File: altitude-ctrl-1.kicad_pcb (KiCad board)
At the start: 2 copper layers, 90 x 90 mm, 93 parts, among them J1 Conn_01x02, J10 Conn_01x02, J11 Conn_01x04, J2 Conn_01x02, J3 Conn_01x05, J4 TC2030, J5 Conn_01x04_Pin, J6 Conn_01x02, J7 Conn_01x05, J8 Conn_01x05, J9 Conn_01x02, SW1 SW_Push, SW2 SW_SPST, SW3 SW_Push, SW4 SW_SPST, SW5 SW_Push, U1 HT753-1, U2 ULN2003A, U3 LM73100, U4 LM73100, U5 MAX6675, U6 STM32F103C8Tx, U7 SN65HVD230, Y1 8M

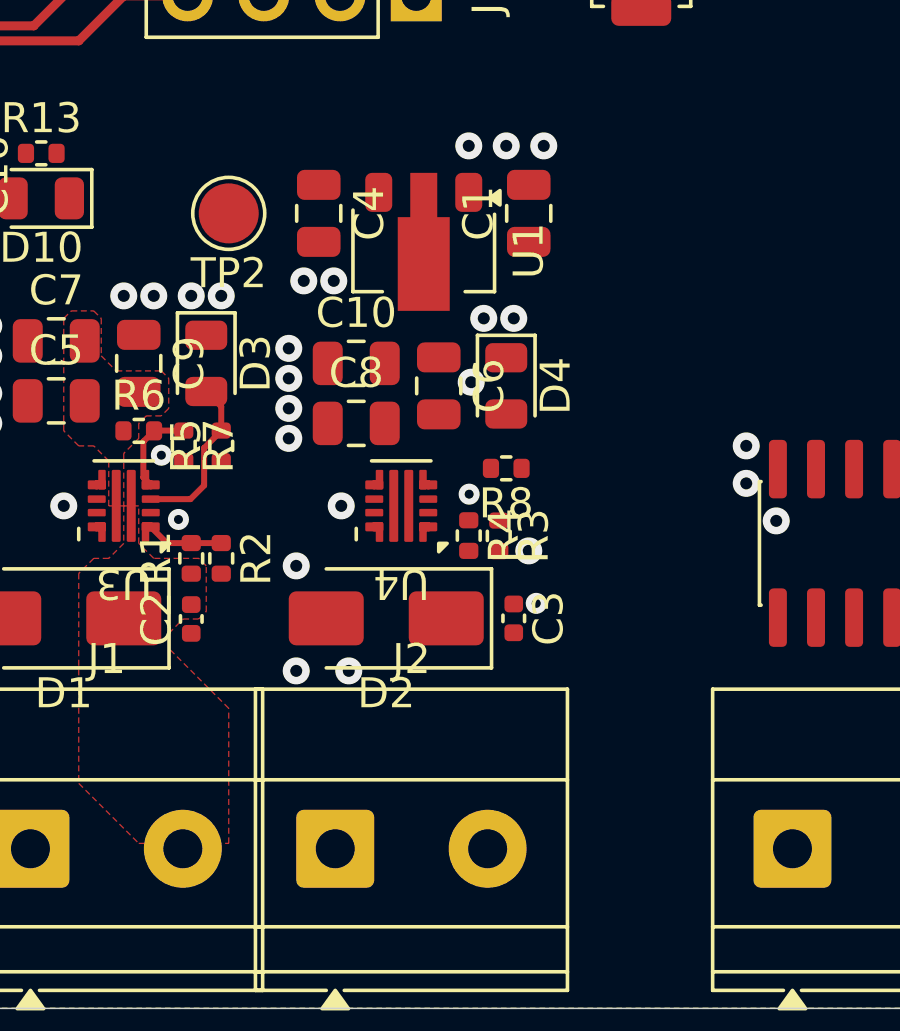
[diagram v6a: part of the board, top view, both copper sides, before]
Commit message: pcb: add +5V input protection routing
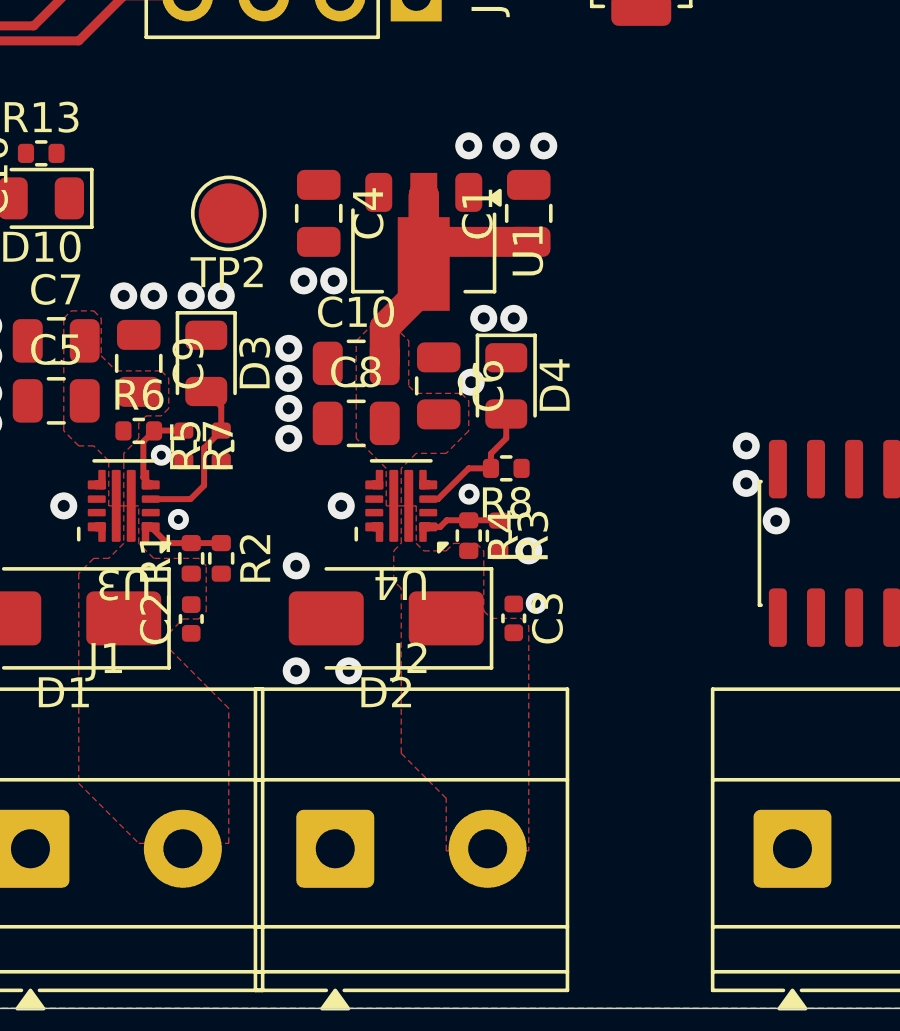
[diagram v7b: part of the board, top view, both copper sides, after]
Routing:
- net +5V: track 0.00 -> 10.9 mm
- net Net-(D4-A): track 0.00 -> 4.54 mm
- net Net-(U4-EN/UVLO): track 0.00 -> 2.45 mm
- added copper zone on F.Cu, net +5V
- added copper zone on F.Cu, net +VCC
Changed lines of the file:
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@@
+	)
+	(segment
+		(start 184.52 102.73)
+		(end 185.25 102.73)
+		(width 0.2)
+		(layer "F.Cu")
+		(net "Net-(U4-EN{slash}UVLO)")
+	)
+	(segment
+		(start 184.3 102.95)
+		(end 184.52 102.73)
+		(width 0.2)
+		(layer "F.Cu")
+		(net "Net-(U4-EN{slash}UVLO)")
+	)
+	(segment
+		(start 186.24 102.73)
+		(end 186.25 102.74)
+		(width 0.2)
+		(layer "F.Cu")
+		(net "Net-(U4-EN{slash}UVLO)")
+	)
+	(segment
+		(start 183.9 102.95)
+		(end 184.3 102.95)
+		(width 0.2)
+		(layer "F.Cu")
+		(net "Net-(U4-EN{slash}UVLO)")
+	)
+	(segment
+		(start 185.25 102.73)
+		(end 186.24 102.73)
+		(width 0.2)
+		(layer "F.Cu")
+		(net "Net-(U4-EN{slash}UVLO)")
+	)
+	(segment
+		(start 185.25 101)
+		(end 185.99 101)
+		(width 0.2)
+		(layer "F.Cu")
+		(net "Net-(D4-A)")
+	)
+	(segment
+		(start 185.99 100.51)
+		(end 186.5 100)
+		(width 0.2)
+		(layer "F.Cu")
+		(net "Net-(D4-A)")
+	)
+	(segment
+		(start 185.99 101)
+		(end 185.99 100.51)
+		(width 0.2)
+		(layer "F.Cu")
+		(net "Net-(D4-A)")
+	)
+	(segment
+		(start 183.9 102.025)
+		(end 184.225 102.025)
+		(width 0.2)
+		(layer "F.Cu")
+		(net "Net-(D4-A)")
+	)
+	(segment
+		(start 184.225 102.025)
+		(end 185.25 101)
+		(width 0.2)
+		(layer "F.Cu")
+		(net "Net-(D4-A)")
+	)
+	(segment
+		(start 186.5 100)
+		(end 186.5 99.1875)
+		(width 0.2)
+		(layer "F.Cu")
+		(net "Net-(D4-A)")
+	)
+	(segment
+		(start 182.45 97.5)
+		(end 182.45 96.3)
+		(width 1)
+		(layer "F.Cu")
+		(net "+5V")
+	)
+	(segment
+		(start 183.75 93)
+		(end 183.75 91.8875)
+		(width 1)
+		(layer "F.Cu")
+		(net "+5V")
+	)
+	(segment
+		(start 183.75 95)
+		(end 183.75 91.8875)
+		(width 1)
+		(layer "F.Cu")
+		(net "+5V")
+	)
+	(segment
+		(start 184.2 93.45)
+		(end 183.75 93)
+		(width 1)
+		(layer "F.Cu")
+		(net "+5V")
+	)
+	(segment
+		(start 182.45 96.3)
+		(end 183.75 95)
+		(width 1)
+		(layer "F.Cu")
+		(net "+5V")
+	)
+	(segment
+		(start 187.25 93.45)
+		(end 184.2 93.45)
+		(width 1)
+		(layer "F.Cu")
+		(net "+5V")
 	)
 	(segment
@@
 	)
 	(zone
+		(net "+5V")
+		(layer "F.Cu")
+		(hatch edge 0.5)
+		(priority 4)
+		(connect_pads yes
+			(clearance 0.2)
+		)
+		(min_thickness 0.15)
+		(fill yes
+			(thermal_gap 0.5)
+			(thermal_bridge_width 0.5)
+			(island_removal_mode 1)
+		)
+		(polygon
+			(pts
+				(xy 183.25 98.25) (xy 183.5 98.5) (xy 185 98.5) (xy 185.25 98.75) (xy 185.25 99.75) (xy 184.5 100.5)
+				(xy 183.5 100.5) (xy 183 101) (xy 183 102.25) (xy 182.5 102.25) (xy 182.5 101) (xy 181.5 100) (xy 181.5 96.75)
+				(xy 182 96.25) (xy 182.75 96.25) (xy 183.25 96.75)
+			)
+		)
+	)
+	(zone
 		(net "+12V_IN")
 		(layer "F.Cu")
@@
 			)
 		)
+	)
+	(zone
+		(net "+VCC")
+		(layer "F.Cu")
+		(hatch edge 0.5)
+		(priority 3)
+		(connect_pads yes
+			(clearance 0.2)
+		)
+		(min_thickness 0.15)
+		(fill yes
+			(thermal_gap 0.5)
+			(thermal_bridge_width 0.5)
+			(island_removal_mode 0)
+		)
+		(polygon
+			(pts
+				(xy 184.5 113.75) (xy 184.5 112) (xy 183 110.5) (xy 183 105) (xy 182.75 104.75) (xy 182.75 103.75)
+				(xy 183 103.5) (xy 183 102.25) (xy 183.5 102.25) (xy 183.5 103.5) (xy 183.75 103.75) (xy 184.5 103.75)
+				(xy 184.75 103.5) (xy 185.5 103.5) (xy 185.75 103.75) (xy 185.75 105.75) (xy 186 106) (xy 187 106)
+				(xy 187.25 106.25) (xy 187.25 113.75)
+			)
+		)

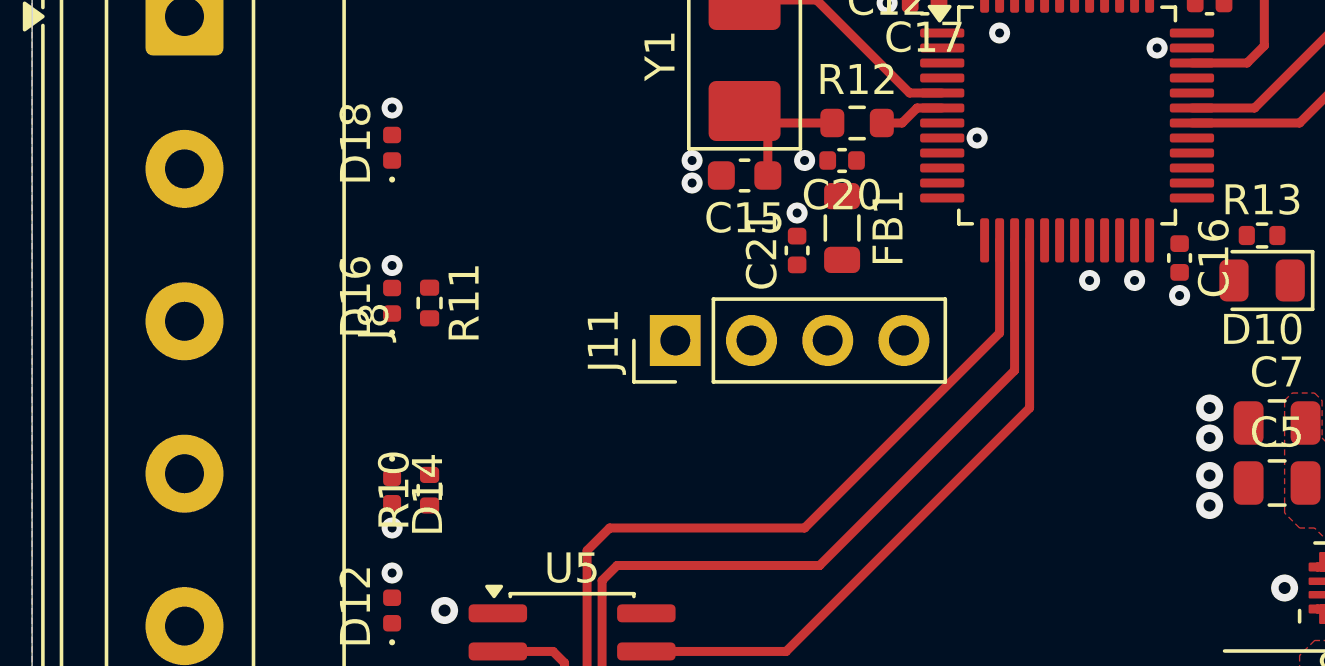
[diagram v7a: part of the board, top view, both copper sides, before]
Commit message: pcb: add i2c routing
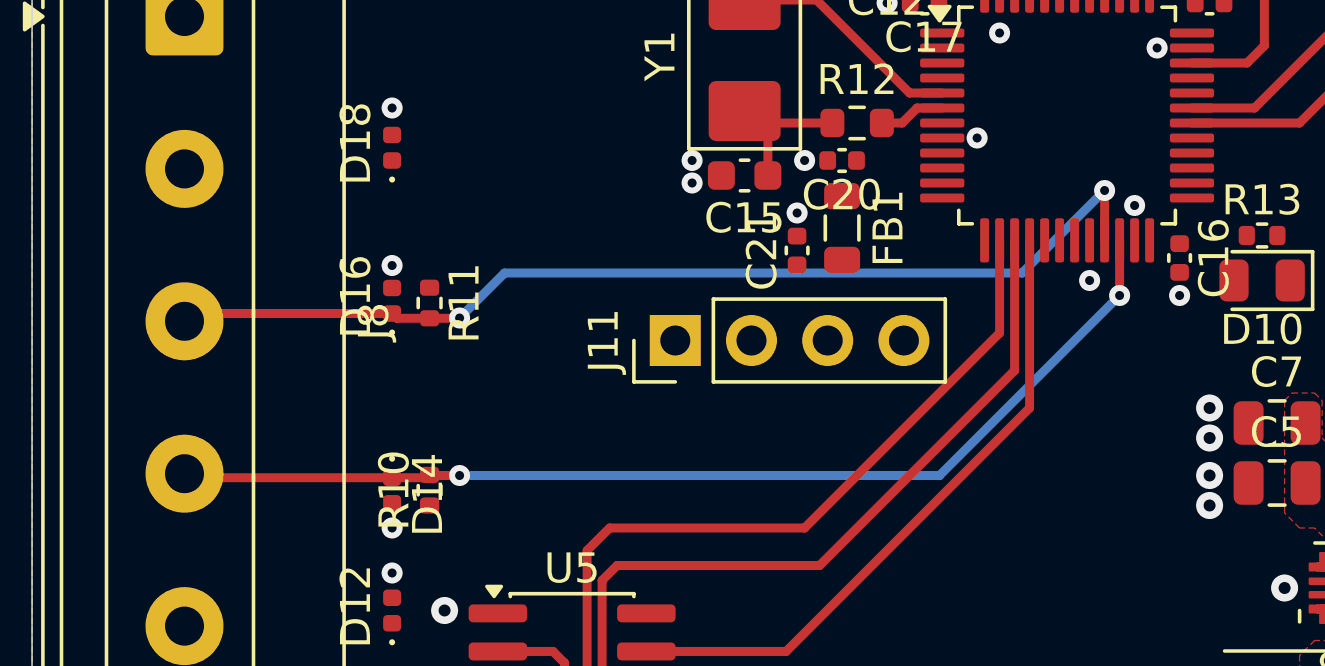
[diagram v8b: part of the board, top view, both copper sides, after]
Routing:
- net /SDA: track 0.00 -> 35.6 mm, vias 0 -> 2
- net /SCL: track 0.00 -> 34.3 mm, vias 0 -> 2
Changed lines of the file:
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@@
 	)
 	(via
-		(at 166.75 92)
+		(at 166.75 89.5)
 		(size 0.7)
 		(drill 0.3)
@@
 	)
 	(segment
+		(start 143.27 98.5)
+		(end 143.25 98.48)
+		(width 0.3)
+		(layer "F.Cu")
+		(net "/SDA")
+	)
+	(segment
+		(start 143.155 98.575)
+		(end 143.25 98.48)
+		(width 0.3)
+		(layer "F.Cu")
+		(net "/SDA")
+	)
+	(segment
+		(start 166.25 90.6625)
+		(end 166.25 92.5)
+		(width 0.3)
+		(layer "F.Cu")
+		(net "/SDA")
+	)
+	(segment
+		(start 142 98.575)
+		(end 143.155 98.575)
+		(width 0.3)
+		(layer "F.Cu")
+		(net "/SDA")
+	)
+	(segment
+		(start 135.08 98.44)
+		(end 135.215 98.575)
+		(width 0.3)
+		(layer "F.Cu")
+		(net "/SDA")
+	)
+	(segment
+		(start 135.215 98.575)
+		(end 142 98.575)
+		(width 0.3)
+		(layer "F.Cu")
+		(net "/SDA")
+	)
+	(segment
+		(start 144.25 98.5)
+		(end 143.27 98.5)
+		(width 0.3)
+		(layer "F.Cu")
+		(net "/SDA")
+	)
+	(via
+		(at 144.25 98.5)
+		(size 0.7)
+		(drill 0.3)
+		(layers "F.Cu" "B.Cu")
+		(net "/SDA")
+	)
+	(via
+		(at 166.25 92.5)
+		(size 0.7)
+		(drill 0.3)
+		(layers "F.Cu" "B.Cu")
+		(net "/SDA")
+	)
+	(segment
+		(start 166.25 92.5)
+		(end 160.25 98.5)
+		(width 0.3)
+		(layer "B.Cu")
+		(net "/SDA")
+	)
+	(segment
+		(start 160.25 98.5)
+		(end 144.25 98.5)
+		(width 0.3)
+		(layer "B.Cu")
+		(net "/SDA")
+	)
+	(segment
 		(start 152 108)
 		(end 148.75 108)
@@
 	)
 	(segment
+		(start 143.25 93.26)
+		(end 144.24 93.26)
+		(width 0.3)
+		(layer "F.Cu")
+		(net "/SCL")
+	)
+	(segment
+		(start 135.34 93.1)
+		(end 135.08 93.36)
+		(width 0.3)
+		(layer "F.Cu")
+		(net "/SCL")
+	)
+	(segment
+		(start 165.75 89)
+		(end 165.75 90.6625)
+		(width 0.3)
+		(layer "F.Cu")
+		(net "/SCL")
+	)
+	(segment
+		(start 144.24 93.26)
+		(end 144.25 93.25)
+		(width 0.3)
+		(layer "F.Cu")
+		(net "/SCL")
+	)
+	(segment
+		(start 142 93.1)
+		(end 135.34 93.1)
+		(width 0.3)
+		(layer "F.Cu")
+		(net "/SCL")
+	)
+	(segment
+		(start 143.25 93.26)
+		(end 142.16 93.26)
+		(width 0.3)
+		(layer "F.Cu")
+		(net "/SCL")
+	)
+	(segment
+		(start 142.16 93.26)
+		(end 142 93.1)
+		(width 0.3)
+		(layer "F.Cu")
+		(net "/SCL")
+	)
+	(via
+		(at 144.25 93.25)
+		(size 0.7)
+		(drill 0.3)
+		(layers "F.Cu" "B.Cu")
+		(net "/SCL")
+	)
+	(via
+		(at 165.75 89)
+		(size 0.7)
+		(drill 0.3)
+		(layers "F.Cu" "B.Cu")
+		(net "/SCL")
+	)
+	(segment
+		(start 145.75 91.75)
+		(end 163 91.75)
+		(width 0.3)
+		(layer "B.Cu")
+		(net "/SCL")
+	)
+	(segment
+		(start 144.25 93.25)
+		(end 145.75 91.75)
+		(width 0.3)
+		(layer "B.Cu")
+		(net "/SCL")
+	)
+	(segment
+		(start 163 91.75)
+		(end 165.75 89)
+		(width 0.3)
+		(layer "B.Cu")
+		(net "/SCL")
+	)
+	(segment
